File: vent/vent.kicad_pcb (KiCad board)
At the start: 2 copper layers, 31 parts, among them J1 Valve Control, J2 CAN Connector, J3 Programming Header, J4 Valve Connection, Q1 Q_NMOS_GDS, U1 INA180, U2 MCP2562, U3 PIC18F26K83, Y1 Crystal

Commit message: Finish layout
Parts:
- added REF**: MountingHole_3mm, MountingHole:MountingHole_3mm, F.Cu at (109.2, 133.3)
- added REF**: MountingHole_3mm, MountingHole:MountingHole_3mm, F.Cu at (149.9, 133.3)
- added REF**: MountingHole_3mm, MountingHole:MountingHole_3mm, F.Cu at (109.2, 101.6)
- added REF**: MountingHole_3mm, MountingHole:MountingHole_3mm, F.Cu at (149.9, 101.6)
- C3, F2, J3, R1, R10, R11, R2, R3, R4, R5, R6, R7, R8, R9, U2: moved to B.Cu
- moved R9 165.7 mm to (137.2, 115.6), turned to 180 degrees
- moved R7 165.4 mm to (124.5, 124.1), turned to 270 degrees
- moved D1 164.6 mm to (142.2, 115.6), turned to 270 degrees
- moved R8 164.2 mm to (137.2, 120.7), turned to 180 degrees
- moved R11 157.9 mm to (144.4, 115.6)
- moved Q1 157.7 mm to (142.2, 127.0)
- moved R10 157.0 mm to (144.4, 120.7)
- moved R5 156.5 mm to (134.6, 124.1), turned to 270 degrees
- moved R6 155.6 mm to (129.5, 124.1), turned to 270 degrees
- moved D4 153.0 mm to (124.5, 128.1), turned to 270 degrees
- moved U2 152.8 mm to (128.3, 118.1), turned to 180 degrees
- moved C5 152.3 mm to (116.5, 113.0)
- moved D2 152.0 mm to (134.6, 128.3), turned to 270 degrees
- moved C4 151.0 mm to (116.5, 108.0), turned to 180 degrees
- moved J4 150.5 mm to (148.6, 114.3), turned to 90 degrees
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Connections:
- U3 pad 11: /MCU/CAN_TX -> /MCU/CAN_RX
- U3 pad 12: /MCU/CAN_RX -> /MCU/CAN_TX

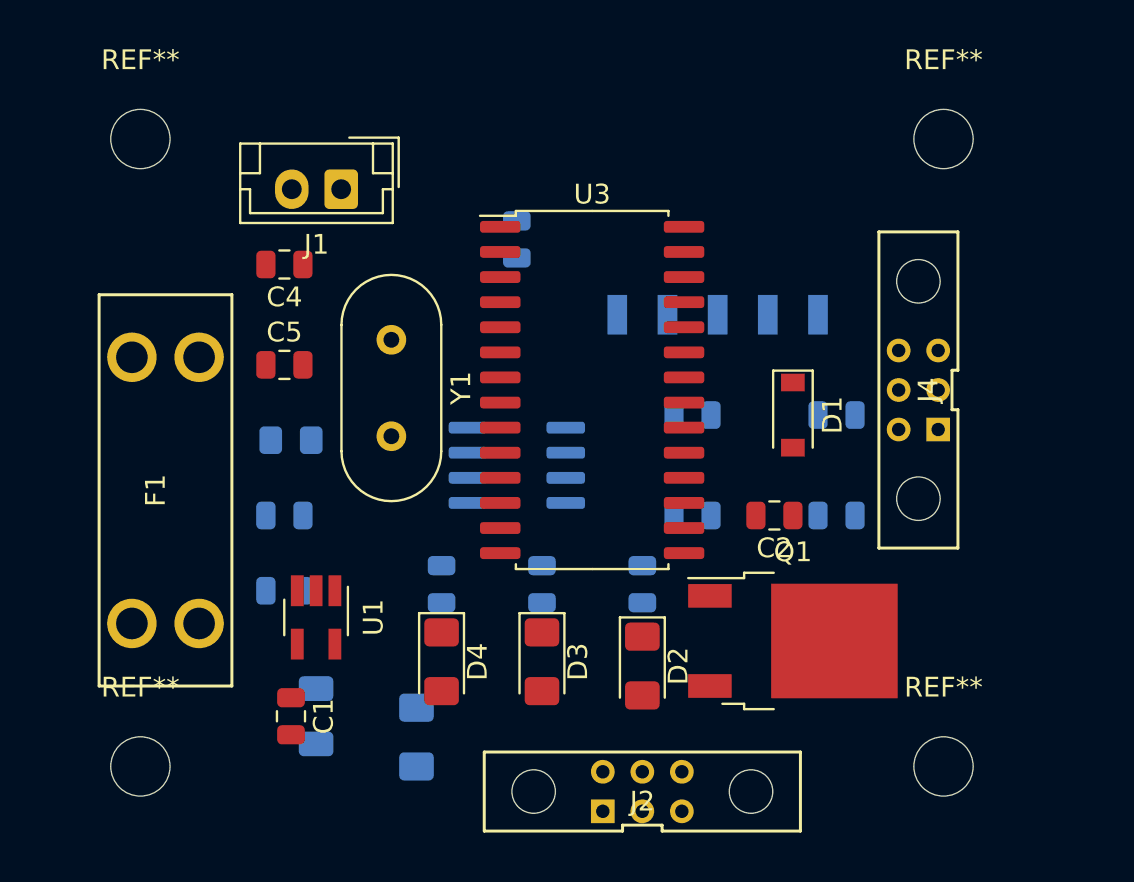
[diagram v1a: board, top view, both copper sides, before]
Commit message: Update layout to adresss review comments
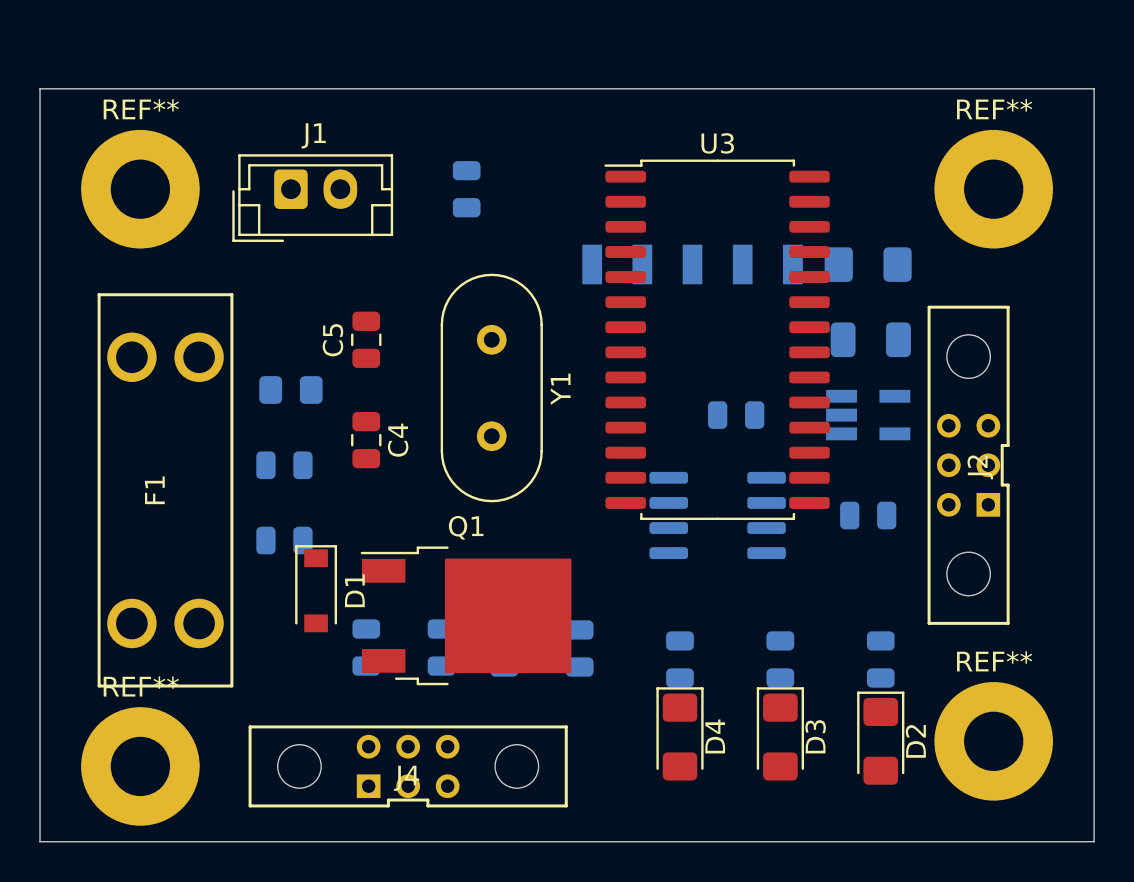
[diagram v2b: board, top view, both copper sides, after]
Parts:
- removed the REF** at (109.2, 133.3)
- removed the REF** at (149.9, 133.3)
- removed the REF** at (109.2, 101.6)
- removed the REF** at (149.9, 101.6)
- added REF**: MountingHole_3mm_Pad, MountingHole:MountingHole_3mm_Pad, F.Cu at (152.4, 104.1)
- added REF**: MountingHole_3mm_Pad, MountingHole:MountingHole_3mm_Pad, F.Cu at (152.4, 132.1)
- added REF**: MountingHole_3mm_Pad, MountingHole:MountingHole_3mm_Pad, F.Cu at (109.2, 133.3)
- added REF**: MountingHole_3mm_Pad, MountingHole:MountingHole_3mm_Pad, F.Cu at (109.2, 104.1)
- C1, C2, U1: moved to B.Cu
- moved R1 33.9 mm to (146.2, 111.8), turned to 180 degrees
- moved F2 33.1 mm to (146.1, 108.0), turned to 0 degrees
- moved J4 32.1 mm to (122.8, 133.3), turned to 0 degrees
- moved C1 30.9 mm to (146.1, 120.7), turned to 0 degrees
- moved U1 29.8 mm to (146.1, 115.6), turned to 0 degrees
- moved R11 26.5 mm to (120.7, 127.3), turned to 270 degrees
- moved D1 25.7 mm to (118.1, 124.5)
- moved J2 23.3 mm to (151.1, 118.1), turned to 90 degrees
- moved R10 21.1 mm to (124.5, 127.3), turned to 270 degrees
- moved Q1 16.6 mm to (125.7, 125.7)
- moved R9 15.2 mm to (127.6, 127.4), turned to 270 degrees
- moved D4 12.7 mm to (136.5, 131.9)
- moved R7 12.7 mm to (136.5, 127.9)
- moved D2 12.7 mm to (146.7, 132.1)
- moved D3 12.7 mm to (141.6, 131.9)
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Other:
- board outline added: 53.3 x 38.1 mm

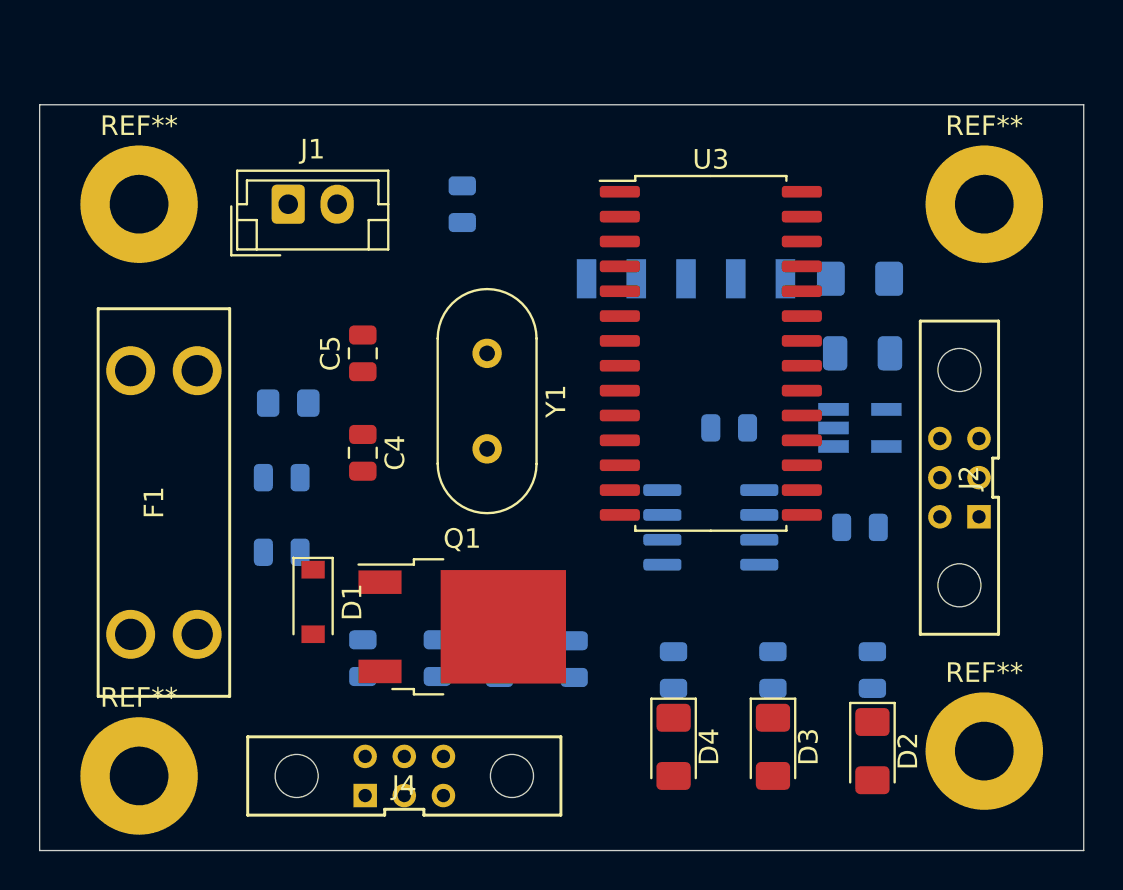
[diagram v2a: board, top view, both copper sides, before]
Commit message: Add third layout, optimize placement for tracing
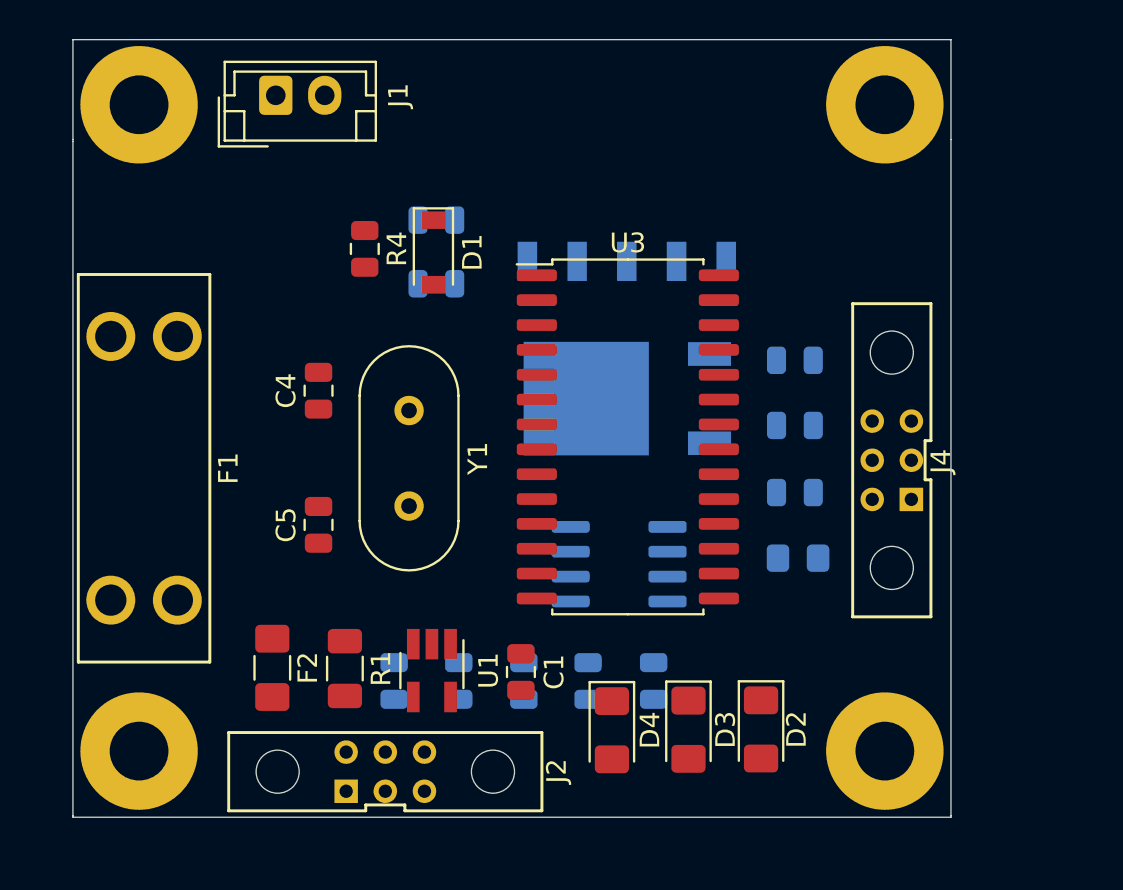
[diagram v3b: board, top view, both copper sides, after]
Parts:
- C1, F2, R1, R4, U1: moved to F.Cu
- Q1: moved to B.Cu
- moved F2 36.0 mm to (116.0, 127.8), turned to 270 degrees
- moved J2 33.0 mm to (121.8, 133.1), turned to 0 degrees
- moved R1 31.0 mm to (119.7, 127.9), turned to 90 degrees
- moved J4 29.7 mm to (147.7, 117.2), turned to 90 degrees
- moved C3 27.2 mm to (142.9, 122.2), turned to 0 degrees
- moved U1 25.1 mm to (124.2, 128.0), turned to 270 degrees
- moved R10 23.8 mm to (142.7, 112.1), turned to 0 degrees
- moved R11 23.6 mm to (142.7, 118.9), turned to 0 degrees
- moved D1 18.9 mm to (124.3, 106.6)
- moved C1 18.8 mm to (128.7, 128.0), turned to 90 degrees
- moved R3 15.8 mm to (124.4, 108.2), turned to 180 degrees
- moved R2 15.3 mm to (124.4, 105.0), turned to 0 degrees
- moved Q1 14.4 mm to (134.2, 114.1), turned to 180 degrees
- moved R5 11.2 mm to (135.5, 128.5), turned to 90 degrees
- moved R6 9.47 mm to (132.2, 128.5), turned to 90 degrees
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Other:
- board size 53.3 x 38.1 mm -> 44.9 x 39.7 mm
- net class Default: clearance 0.2 -> 0.1524; trace_width 0.25 -> 0.2032
- rule trace_clearance: 0.2 -> 0.1524
- rule trace_min: 0.2 -> 0.1524

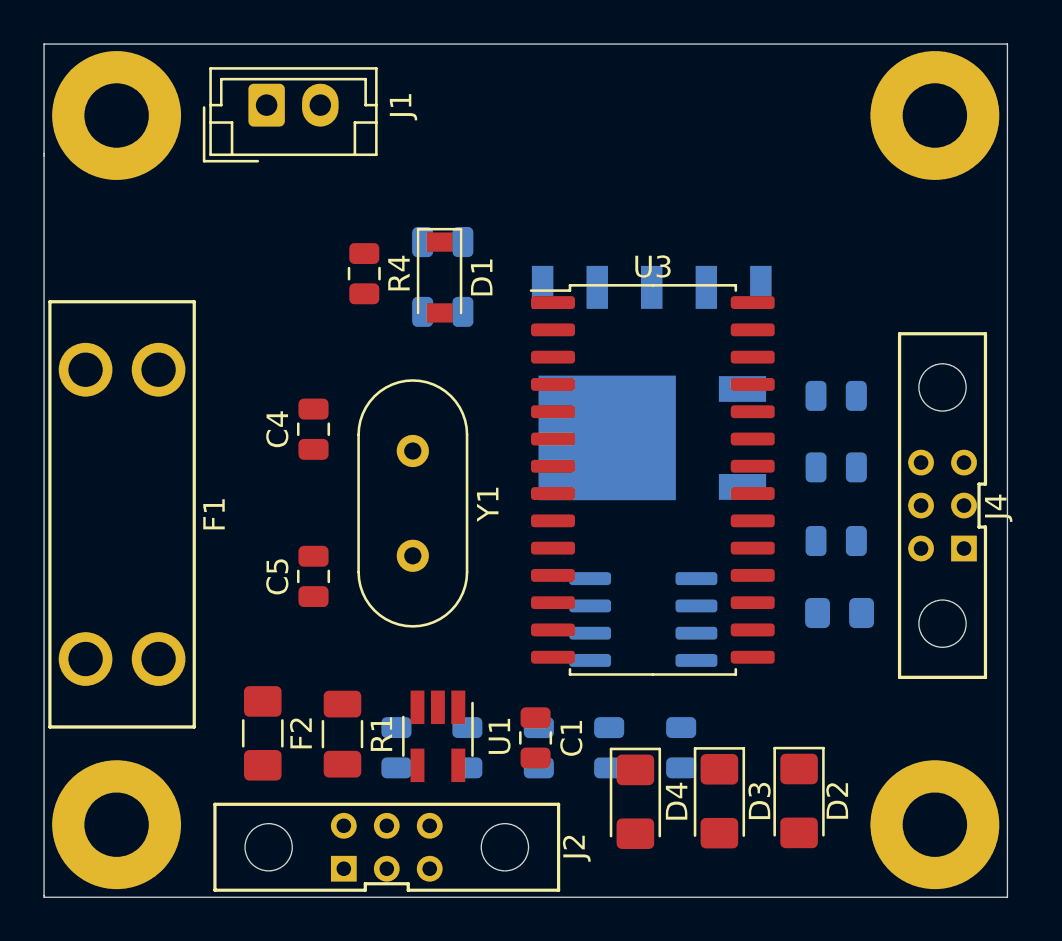
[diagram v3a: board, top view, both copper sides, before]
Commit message: Add pours, Change all dimensions to Eco.User1
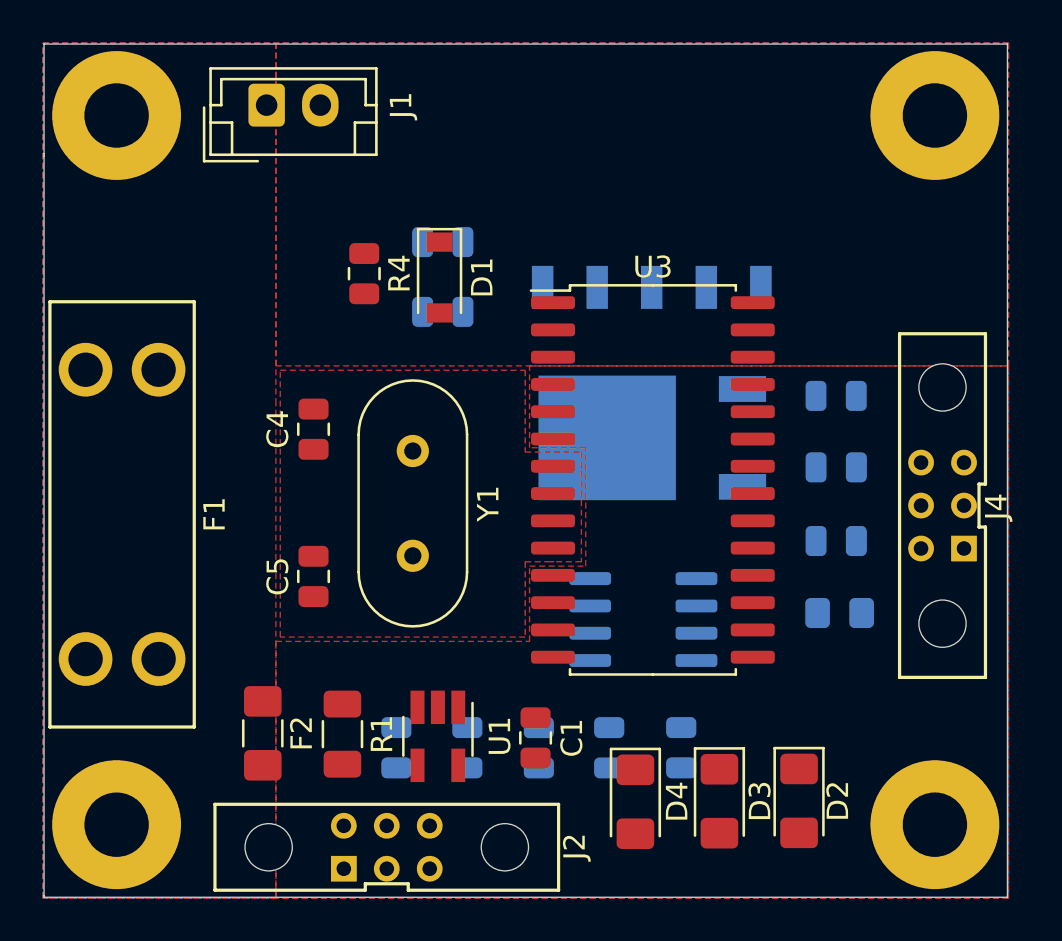
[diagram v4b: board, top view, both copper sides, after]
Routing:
- added copper zone on F.Cu, net +5V
- added copper zone on B.Cu, net GND
- added copper zone on F.Cu, net GND
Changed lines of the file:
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@@
     (thickness 1.6)
     (drawings 11)
-    (tracks 0)
+    (tracks 1)
     (zones 0)
     (modules 35)
@@
   (gr_line (start 150.6982 135.4582) (end 105.8418 135.4582) (layer Edge.Cuts) (width 0.05))
   (gr_line (start 150.6982 100.838) (end 150.6982 135.382) (layer Edge.Cuts) (width 0.05))
+  (segment (start 131.5974 107.061) (end 131.5974 107.0356) (width 0.2032) (layer B.Cu) (net 1))
+  (zone (net 2) (net_name GND) (layer F.Cu) (hatch edge 0.508)
+    (connect_pads (clearance 0.1524))
+    (min_thickness 0.254)
+    (fill yes (arc_segments 32) (thermal_gap 0.508) (thermal_bridge_width 0.508))
+    (polygon
+      (pts
+        (xy 129.413 119.8372) (xy 128.2446 119.8372) (xy 128.2446 123.3424) (xy 116.84 123.3424) (xy 116.84 110.9218)
+        (xy 128.2446 110.9218) (xy 128.2446 114.7318) (xy 130.8608 114.7318) (xy 130.8608 119.8118) (xy 130.8608 119.8372)
+        (xy 129.5908 119.8372) (xy 129.4384 119.8372)
+      )
+    )
+  )
+  (zone (net 2) (net_name GND) (layer B.Cu) (hatch edge 0.508)
+    (connect_pads (clearance 0.1524))
+    (min_thickness 0.254)
+    (fill yes (arc_segments 32) (thermal_gap 0.508) (thermal_bridge_width 0.508))
+    (polygon
+      (pts
+        (xy 105.791 95.6818) (xy 150.749 95.6818) (xy 150.749 135.509) (xy 105.791 135.509)
+      )
+    )
+  )
+  (zone (net 1) (net_name +5V) (layer F.Cu) (hatch edge 0.508)
+    (connect_pads (clearance 0.1524))
+    (min_thickness 0.254)
+    (fill yes (arc_segments 32) (thermal_gap 0.508) (thermal_bridge_width 0.508))
+    (polygon
+      (pts
+        (xy 116.6368 112.3188) (xy 116.6368 135.509) (xy 105.791 135.509) (xy 105.791 95.6818) (xy 116.6368 95.6818)
+      )
+    )
+  )
+  (zone (net 1) (net_name +5V) (layer F.Cu) (hatch edge 0.508)
+    (connect_pads (clearance 0.1524))
+    (min_thickness 0.254)
+    (fill yes (arc_segments 32) (thermal_gap 0.508) (thermal_bridge_width 0.508))
+    (polygon
+      (pts
+        (xy 116.6368 110.7186) (xy 150.749 110.7186) (xy 150.749 95.6818) (xy 116.6368 95.6818)
+      )
+    )
+  )
+  (zone (net 1) (net_name +5V) (layer F.Cu) (hatch edge 0.508)
+    (connect_pads (clearance 0.1524))
+    (min_thickness 0.254)
+    (fill yes (arc_segments 32) (thermal_gap 0.508) (thermal_bridge_width 0.508))
+    (polygon
+      (pts
+        (xy 116.6368 135.509) (xy 116.6368 123.5456) (xy 128.4478 123.5456) (xy 128.4478 120.0404) (xy 131.064 120.0404)
+        (xy 131.064 114.5286) (xy 128.4478 114.5286) (xy 128.4478 110.7186) (xy 150.749 110.7186) (xy 150.749 135.509)
+      )
+    )
+  )
 )

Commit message: Add initial tracing
Definitely not super happy with the first round but I wanted something
to get out for review so we can get this started. I mentioned in slack
we needed an actual part number but it won't affect the number of pads
on Q1 so it should be easy to replace even if the footprint changes.
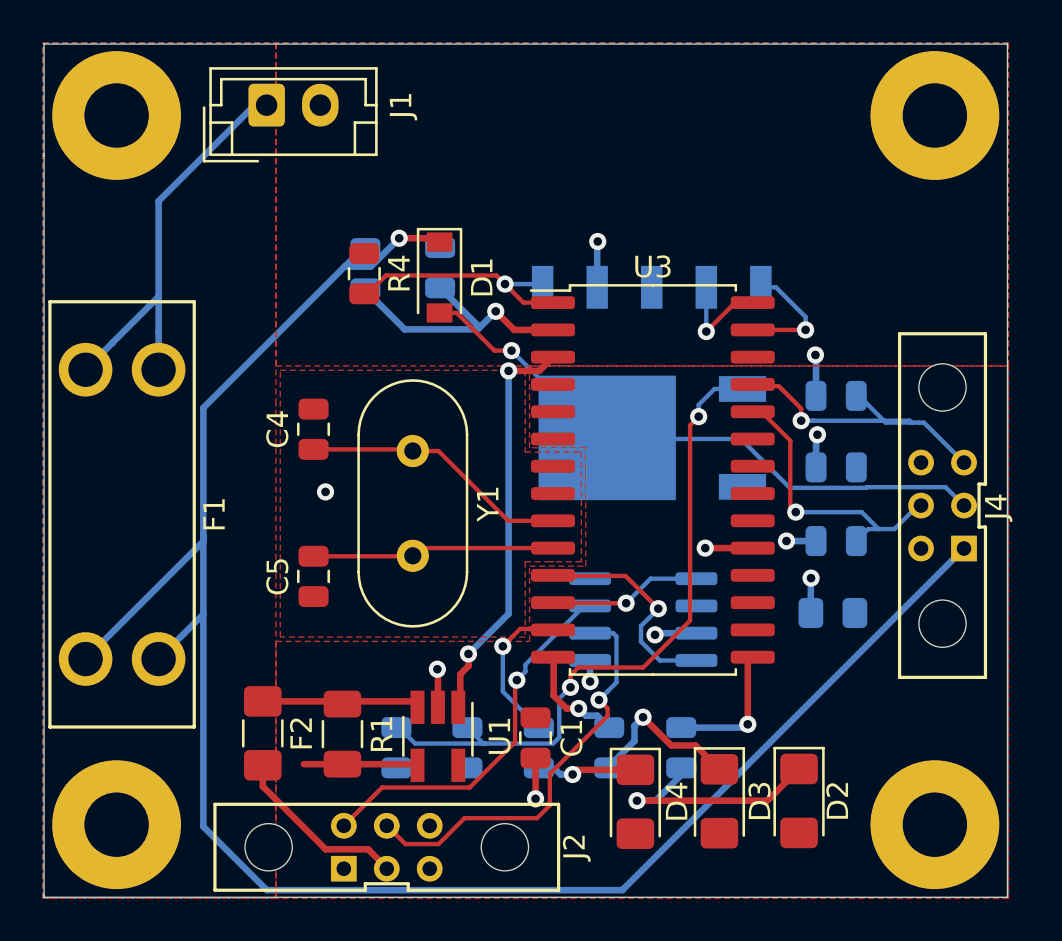
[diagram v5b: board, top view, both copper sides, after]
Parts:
- moved R2 3.81 mm to (120.8, 106.2), turned to 270 degrees
- moved R3 2.06 mm to (124.3, 106.1), turned to 90 degrees
- moved C3 0.31 mm to (142.6, 122.2)
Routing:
- net +12V: track 0.00 -> 89.4 mm, vias 0 -> 1
- net Net-(Q1-Pad1): track 0.00 -> 31.2 mm, vias 0 -> 2
- net /Valve Control/RELAY-: track 0.00 -> 25.8 mm, vias 0 -> 1
- net Net-(F1-Pad2): track 0.00 -> 19.9 mm
- net CANL: track 0.00 -> 19.5 mm, vias 0 -> 1
- net /MCU/CURR_AMP: track 0.00 -> 19.1 mm, vias 0 -> 2
- net CANH: track 0.00 -> 17.2 mm, vias 0 -> 1
- net +5V: track 0.03 -> 17.0 mm, vias 0 -> 7
- net /MCU/LIMIT_OPEN: track 0.00 -> 14.9 mm, vias 0 -> 1
- net /MCU/LIMIT_CLOSE: track 0.00 -> 13.3 mm, vias 0 -> 1
- net /MCU/OSC1: track 0.00 -> 13.3 mm
- net /MCU/VBAT: track 0.00 -> 12.8 mm, vias 0 -> 1
- net /MCU/~MCLR: track 0.00 -> 11.5 mm, vias 0 -> 1
- net /MCU/OSC2: track 0.00 -> 11.2 mm
- net Net-(D2-Pad1): track 0.00 -> 11.0 mm, vias 0 -> 1
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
